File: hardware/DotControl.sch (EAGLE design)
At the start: 43 parts, among them CN1 1X4-BIG, J3 USB-MICROB, SW2 Previous, SW5 Previous, SW6 Next, SW8 Ok, U1 ATMEGA328P-MU-QFN32, U2 TMP102, U3 ATSHA204-TSU, U4 SI7021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

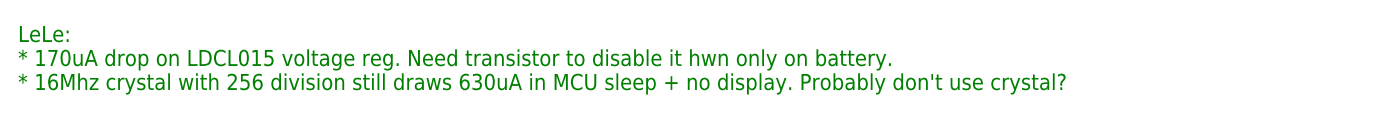
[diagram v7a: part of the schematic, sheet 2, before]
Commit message: Add pulldown on ENA pin of voltage reg to prevent 150uA quiescent current
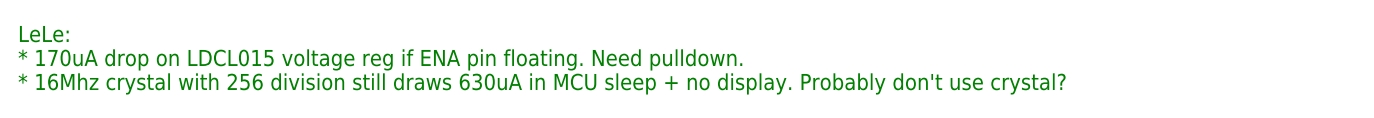
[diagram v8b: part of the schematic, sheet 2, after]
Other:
- note added: "LeLe: * 170uA drop on LDCL015 voltage reg if ENA pin floating. Need pulldown. * 16Mhz crystal with 256 division still draws 630uA in MCU sleep + no display. Probably don't use crystal?"
- note removed: "LeLe: * 170uA drop on LDCL015 voltage reg. Need transistor to disable it hwn only on battery. * 16Mhz crystal with 256 division still draws 630uA in MCU sleep + no display. Probably don't use crystal?"
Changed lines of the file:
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@@
 <plain>
 <text x="-17.78" y="86.36" size="1.778" layer="91">LeLe:
-* 170uA drop on LDCL015 voltage reg. Need transistor to disable it hwn only on battery.
+* 170uA drop on LDCL015 voltage reg if ENA pin floating. Need pulldown.
 * 16Mhz crystal with 256 division still draws 630uA in MCU sleep + no display. Probably don't use crystal?</text>
 </plain>
